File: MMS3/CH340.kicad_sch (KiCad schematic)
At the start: 0 parts

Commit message: backup commit
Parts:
- added C14, C15: 20pF, PCM_JLCPCB:C_0402, symbol PCM_JLCPCB-Capacitors:0402,20pF
- added C23, C54: 100nF, PCM_JLCPCB:C_0402, symbol PCM_JLCPCB-Capacitors:0402,100nF
- added Q1, Q2: MMBT3904 100-300, PCM_JLCPCB:Q_SOT-23, symbol PCM_JLCPCB-Transistors:NPN,MMBT3904 100-300
- added R28, R29: 10kΩ, PCM_JLCPCB:R_0402, symbol PCM_JLCPCB-Resistors:0402,10kΩ
- added U13: CH340G, PCM_JLCPCB:SOIC-16_3.9x9.9mm_P1.27mm, symbol PCM_JLCPCB-Extended:USB-Serial, CH340G
- added X3: X322512MSB4SI, PCM_JLCPCB:CRYSTAL-SMD_4P-L3.2-W2.5-BL, symbol PCM_JLCPCB-Crystals:Crystal, 12MHz, 20pF
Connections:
- new net: Q2.1 (B), R29.2
- new net: Q1.1 (B), R28.2
- new net +3V3: C23.1, C54.1, U13.16 (VCC), U13.4 (V3)
- new net EN: Q1.3 (C)
- new net GND: C14.2, C15.2, C23.2, C54.2, U13.1 (GND), X3.2 (GND), X3.4 (GND)
- new net IO_9: Q2.3 (C)
- new net Prg.D+: U13.5 (UD+)
- new net Prg.D-: U13.6 (UD-)
- new net Prg.RX: U13.3 (RXD)
- new net Prg.TX: U13.2 (TXD)
- new net XI: C14.1, U13.7 (XI), X3.1 (OSC)
- new net XO: C15.1, U13.8 (XO), X3.3 (OSC)
- new net ~{DTR}: Q2.2 (E), R28.1, U13.13 (~{DTR})
- new net ~{RTS}: Q1.2 (E), R29.1, U13.14 (~{RTS})
- no-connect marks 0 -> 5
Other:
- note added: "EN and Boot0 sequencing"
- note added: "UART Flip here"

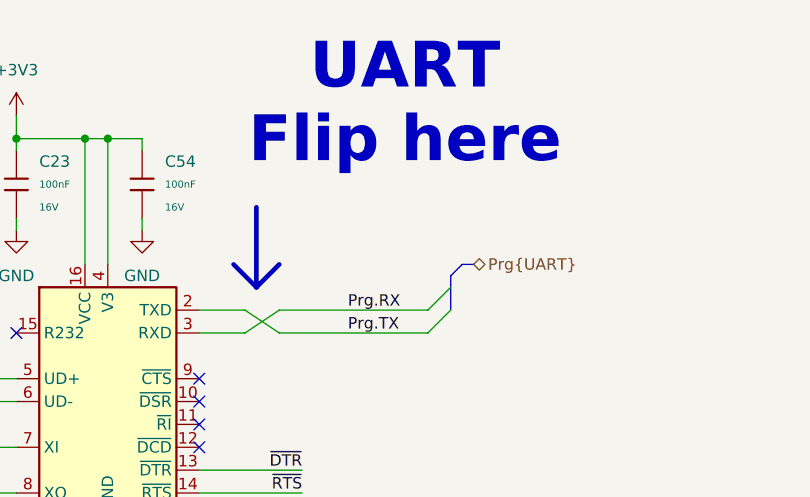
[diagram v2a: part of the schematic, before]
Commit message: fixed swapped RX/TX & D+/D_
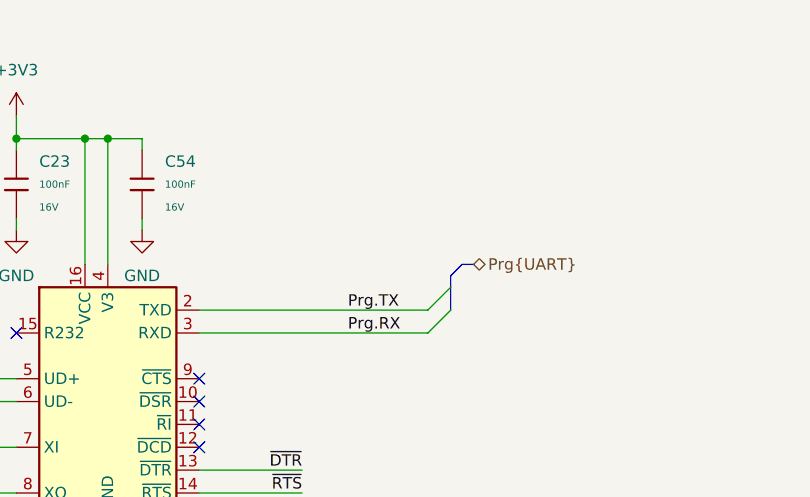
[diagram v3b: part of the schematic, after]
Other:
- note removed: "UART Flip here"
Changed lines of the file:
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@@
 		(comment 2 "DESIGNED IN POLAND")
-	)
-	(text "UART\nFlip here"
-		(exclude_from_sim no)
-		(at 127 41.91 0)
-		(effects
-			(font
-				(size 5.08 5.08)
-				(thickness 1.016)
-				(bold yes)
-			)
-		)
 	)
 	(text "EN and Boot0 sequencing"
@@
 	(wire
 		(pts
-			(xy 104.14 64.77) (xy 109.22 64.77)
-		)
-		(stroke
-			(width 0)
-			(type default)
-		)
-	)
-	(wire
-		(pts
-			(xy 113.03 67.31) (xy 109.22 64.77)
-		)
-		(stroke
-			(width 0)
-			(type default)
-		)
-	)
-	(wire
-		(pts
-			(xy 113.03 64.77) (xy 129.54 64.77)
+			(xy 104.14 64.77) (xy 129.54 64.77)
 		)
 		(stroke
@@
 		)
 	)
-	(polyline
-		(pts
-			(xy 110.49 62.23) (xy 113.03 59.69)
-		)
-		(stroke
-			(width 0.508)
-			(type default)
-		)
-	)
 	(wire
 		(pts
@@
 	(wire
 		(pts
-			(xy 104.14 67.31) (xy 109.22 67.31)
-		)
-		(stroke
-			(width 0)
-			(type default)
-		)
-	)
-	(wire
-		(pts
-			(xy 113.03 67.31) (xy 129.54 67.31)
+			(xy 104.14 67.31) (xy 129.54 67.31)
 		)
 		(stroke
@@
 		)
 	)
-	(polyline
-		(pts
-			(xy 110.49 53.34) (xy 110.49 62.23)
-		)
-		(stroke
-			(width 0.508)
-			(type default)
-		)
-	)
 	(bus
 		(pts
@@
 	(wire
 		(pts
-			(xy 109.22 67.31) (xy 113.03 64.77)
-		)
-		(stroke
-			(width 0)
-			(type default)
-		)
-	)
-	(wire
-		(pts
 			(xy 78.74 111.76) (xy 82.55 111.76)
 		)
@@
 		(stroke
 			(width 0)
-			(type default)
-		)
-	)
-	(polyline
-		(pts
-			(xy 107.95 59.69) (xy 110.49 62.23)
-		)
-		(stroke
-			(width 0.508)
 			(type default)
 		)
@@
 	)
 	(label "Prg.TX"
-		(at 120.65 67.31 0)
+		(at 120.65 64.77 0)
 		(effects
 			(font
@@
 	)
 	(label "Prg.RX"
-		(at 120.65 64.77 0)
-		(effects
-			(font
+		(at 120.65 67.31 0)
+		(effects
+			(font
